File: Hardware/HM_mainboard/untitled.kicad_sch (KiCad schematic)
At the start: 19 parts, among them J1 JST PH2P ST90, Q1 PMOS AS3401, U1 MCP73831-2, U2 TC1262-33

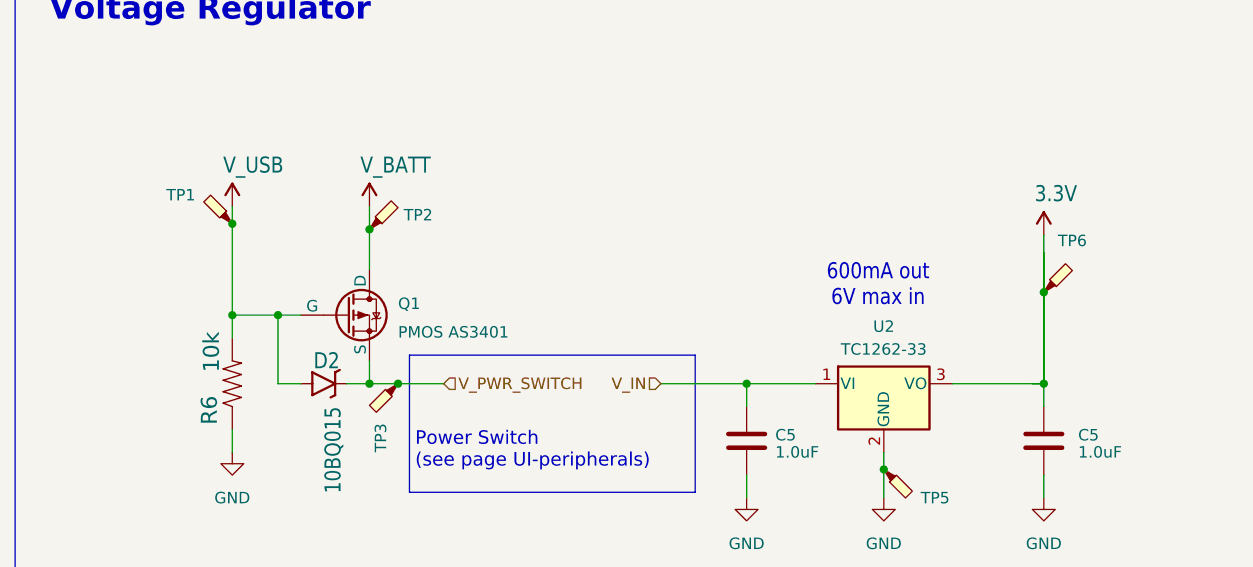
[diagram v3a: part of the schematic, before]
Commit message: Updated schematic to version v2.0.0
•	Removed two 6-Axis IMUs
•	As the BNO055 did not respond to I2C requests, a 2k7 pullup was added in parallel to the I2C-SDA pullup. The behavior is described here:  https://forums.adafruit.com/viewtopic.php?t=205215
•	Added mounting holes for enclosure
•	Added board description prints
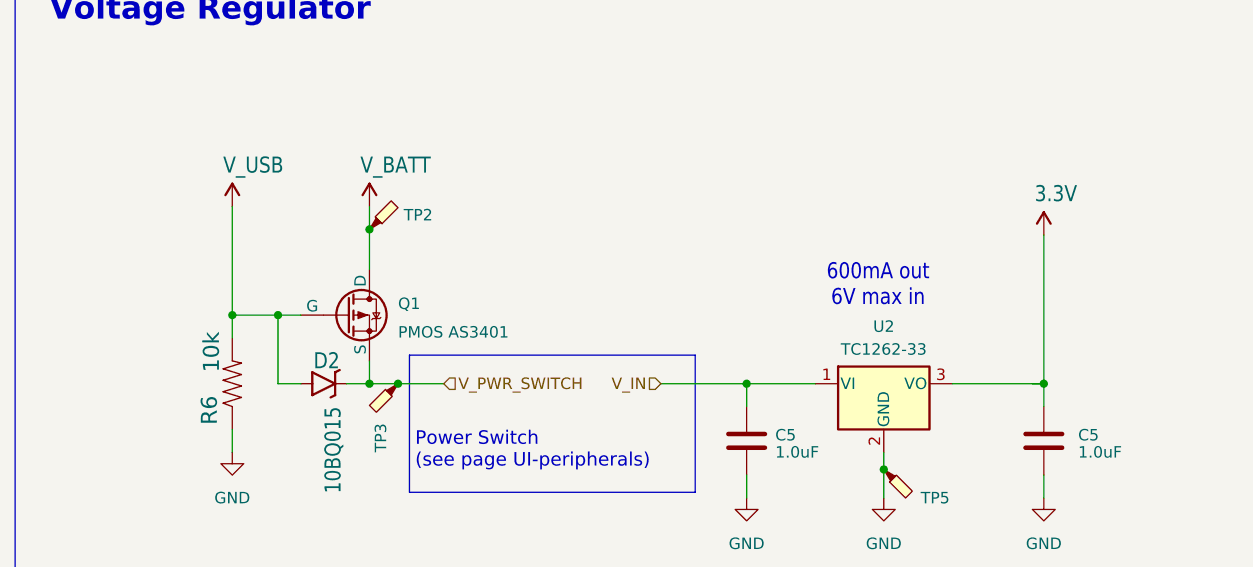
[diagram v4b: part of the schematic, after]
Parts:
- removed TP1: TestPoint_Probe, TestPoint:TestPoint_THTPad_D2.0mm_Drill1.0mm, symbol Connector:TestPoint_Probe
- removed TP6: 3v3, TestPoint:TestPoint_THTPad_D2.0mm_Drill1.0mm, symbol Connector:TestPoint_Probe
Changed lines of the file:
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@@
   (junction (at 109.855 149.86) (diameter 0) (color 0 0 0 0)
   )
-  (junction (at 44.45 47.625) (diameter 0) (color 0 0 0 0)
-  )
   (junction (at 59.69 65.405) (diameter 0) (color 0 0 0 0)
   )
@@
   (junction (at 49.53 57.785) (diameter 0) (color 0 0 0 0)
   )
-  (junction (at 134.62 55.245) (diameter 0) (color 0 0 0 0)
-  )
   (wire (pts (xy 63.5 155.575) (xy 65.405 155.575))
     (stroke (width 0) (type default))
@@
     (stroke (width 0) (type default))
   )
-  (wire (pts (xy 44.45 45.72) (xy 44.45 47.625))
-    (stroke (width 0.1524) (type solid))
-  )
-  (wire (pts (xy 44.45 47.625) (xy 44.45 57.785))
+  (wire (pts (xy 44.45 45.72) (xy 44.45 57.785))
     (stroke (width 0.1524) (type solid))
   )
@@
     (stroke (width 0.1524) (type solid))
   )
-  (wire (pts (xy 134.62 65.405) (xy 134.62 55.245))
-    (stroke (width 0.1524) (type solid))
-  )
   (wire (pts (xy 101.6 65.405) (xy 109.22 65.405))
     (stroke (width 0.1524) (type solid))
@@
     (stroke (width 0.1524) (type solid))
   )
-  (wire (pts (xy 134.62 48.895) (xy 134.62 55.245))
-    (stroke (width 0.1524) (type solid))
-  )
   (wire (pts (xy 134.62 65.405) (xy 133.35 65.405))
     (stroke (width 0) (type default))
@@
     (stroke (width 0) (type default))
   )
-  (wire (pts (xy 134.62 55.245) (xy 134.62 50.8))
-    (stroke (width 0) (type default))
-  )
   (wire (pts (xy 134.62 78.105) (xy 134.62 75.565))
     (stroke (width 0.1524) (type solid))
@@
     (stroke (width 0) (type default))
   )
-  (wire (pts (xy 134.62 55.245) (xy 134.62 65.405))
+  (wire (pts (xy 134.62 48.895) (xy 134.62 65.405))
     (stroke (width 0) (type default))
   )
@@
         )
         (path "/54a6df43-5475-46a2-9916-8b0260700d4c/b19d5209-4861-4a96-a3d1-daca4a23de52"
-          (reference "#SUPPLY026") (unit 1)
+          (reference "#SUPPLY03") (unit 1)
         )
       )
@@
         )
         (path "/54a6df43-5475-46a2-9916-8b0260700d4c/b19d5209-4861-4a96-a3d1-daca4a23de52"
-          (reference "#PWR08") (unit 1)
+          (reference "#PWR07") (unit 1)
         )
       )
@@
         )
         (path "/54a6df43-5475-46a2-9916-8b0260700d4c/b19d5209-4861-4a96-a3d1-daca4a23de52"
-          (reference "#PWR06") (unit 1)
+          (reference "#PWR05") (unit 1)
         )
       )
@@
         )
         (path "/54a6df43-5475-46a2-9916-8b0260700d4c/b19d5209-4861-4a96-a3d1-daca4a23de52"
-          (reference "#PWR04") (unit 1)
+          (reference "#PWR03") (unit 1)
         )
       )
@@
         )
         (path "/54a6df43-5475-46a2-9916-8b0260700d4c/b19d5209-4861-4a96-a3d1-daca4a23de52"
-          (reference "#PWR010") (unit 1)
+          (reference "#PWR09") (unit 1)
         )
       )
@@
         )
         (path "/54a6df43-5475-46a2-9916-8b0260700d4c/b19d5209-4861-4a96-a3d1-daca4a23de52"
-          (reference "#PWR09") (unit 1)
+          (reference "#PWR08") (unit 1)
         )
       )
@@
         )
         (path "/54a6df43-5475-46a2-9916-8b0260700d4c/b19d5209-4861-4a96-a3d1-daca4a23de52"
-          (reference "#PWR07") (unit 1)
+          (reference "#PWR06") (unit 1)
         )
       )
@@
         )
         (path "/54a6df43-5475-46a2-9916-8b0260700d4c/b19d5209-4861-4a96-a3d1-daca4a23de52"
-          (reference "#PWR05") (unit 1)
+          (reference "#PWR04") (unit 1)
         )
       )
@@
     )
   )
-  (symbol (lib_id "Connector:TestPoint_Probe") (at 134.62 55.245 0) (unit 1)
-    (in_bom yes) (on_board yes) (dnp no)
-    (property "Reference" "TP6" (at 137.795 49.53 0)
-      (effects (font (size 1.27 1.27)))
-    )
-    (property "Value" "3v3" (at 135.89 49.53 0)
-      (effects (font (size 1.27 1.27)) hide)
-    )
-    (property "Footprint" "TestPoint:TestPoint_THTPad_D2.0mm_Drill1.0mm" (at 139.7 55.245 0)
-      (effects (font (size 1.27 1.27)) hide)
-    )
-    (property "Datasheet" "~" (at 139.7 55.245 0)
-      (effects (font (size 1.27 1.27)) hide)
-    )
-    (pin "1")
-    (instances
-      (project "HM_mainboard"
-        (path "/54a6df43-5475-46a2-9916-8b0260700d4c/b19d5209-4861-4a96-a3d1-daca4a23de52"
-          (reference "TP6") (unit 1)
-        )
-      )
-    )
-  )
   (symbol (lib_id "Connector:TestPoint_Probe") (at 59.69 48.26 0) (unit 1)
     (in_bom yes) (on_board yes) (dnp no) (fields_autoplaced)
@@
         )
       )
-    )
-  )
-  (symbol (lib_id "Connector:TestPoint_Probe") (at 44.45 47.625 90) (unit 1)
-    (in_bom yes) (on_board yes) (dnp no)
-    (property "Reference" "TP1" (at 38.735 44.45 90)
-      (effects (font (size 1.27 1.27)))
-    )
-    (property "Value" "TestPoint_Probe" (at 33.02 46.355 90)
-      (effects (font (size 1.27 1.27)) hide)
-    )
-    (property "Footprint" "TestPoint:TestPoint_THTPad_D2.0mm_Drill1.0mm" (at 44.45 42.545 0)
-      (effects (font (size 1.27 1.27)) hide)
-    )
-    (property "Datasheet" "~" (at 44.45 42.545 0)
-      (effects (font (size 1.27 1.27)) hide)
-    )
-    (pin "1")
-    (instances
-      (project "HM_mainboard"
-        (path "/54a6df43-5475-46a2-9916-8b0260700d4c/b19d5209-4861-4a96-a3d1-daca4a23de52"
-          (reference "TP1") (unit 1)
-        )
-      )

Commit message: Added BOM, PDF and zipped V2.0.0 project data
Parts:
- removed TP3: TestPoint_Probe, TestPoint:TestPoint_THTPad_D2.0mm_Drill1.0mm, symbol Connector:TestPoint_Probe
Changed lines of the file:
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@@
   (junction (at 59.69 48.26) (diameter 0) (color 0 0 0 0)
   )
-  (junction (at 62.865 65.405) (diameter 0) (color 0 0 0 0)
-  )
   (junction (at 200.66 138.43) (diameter 0) (color 0 0 0 0)
   )
@@
     (stroke (width 0) (type default))
   )
-  (wire (pts (xy 62.865 65.405) (xy 67.945 65.405))
+  (wire (pts (xy 59.69 65.405) (xy 67.945 65.405))
     (stroke (width 0) (type default))
   )
@@
   (wire (pts (xy 82.55 149.86) (xy 82.55 153.67))
     (stroke (width 0.1524) (type solid))
-  )
-  (wire (pts (xy 59.69 65.405) (xy 62.865 65.405))
-    (stroke (width 0) (type default))
   )
   (wire (pts (xy 59.69 62.865) (xy 59.69 65.405))
@@
         )
       )
-    )
-  )
-  (symbol (lib_id "Connector:TestPoint_Probe") (at 62.865 65.405 180) (unit 1)
-    (in_bom yes) (on_board yes) (dnp no)
-    (property "Reference" "TP3" (at 60.96 73.025 90)
-      (effects (font (size 1.27 1.27)) (justify right))
-    )
-    (property "Value" "TestPoint_Probe" (at 62.865 84.455 90)
-      (effects (font (size 1.27 1.27)) (justify right) hide)
-    )
-    (property "Footprint" "TestPoint:TestPoint_THTPad_D2.0mm_Drill1.0mm" (at 57.785 65.405 0)
-      (effects (font (size 1.27 1.27)) hide)
-    )
-    (property "Datasheet" "~" (at 57.785 65.405 0)
-      (effects (font (size 1.27 1.27)) hide)
-    )
-    (pin "1")
-    (instances
-      (project "HM_mainboard"
-        (path "/54a6df43-5475-46a2-9916-8b0260700d4c/b19d5209-4861-4a96-a3d1-daca4a23de52"
-          (reference "TP3") (unit 1)
-        )
-      )

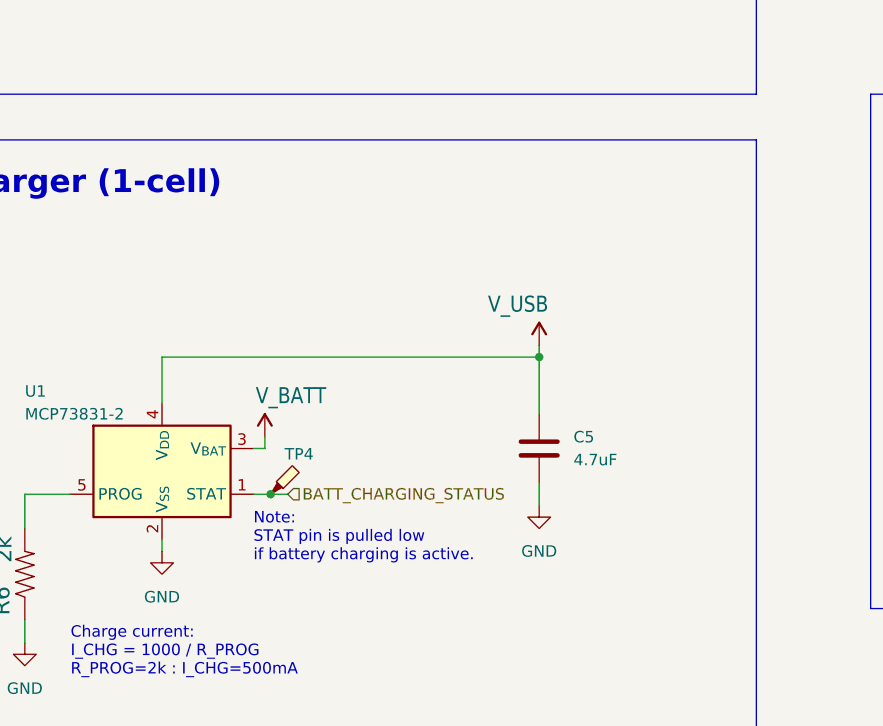
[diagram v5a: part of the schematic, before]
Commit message: Replaced weak pullup at battery charging status by 1k pullup
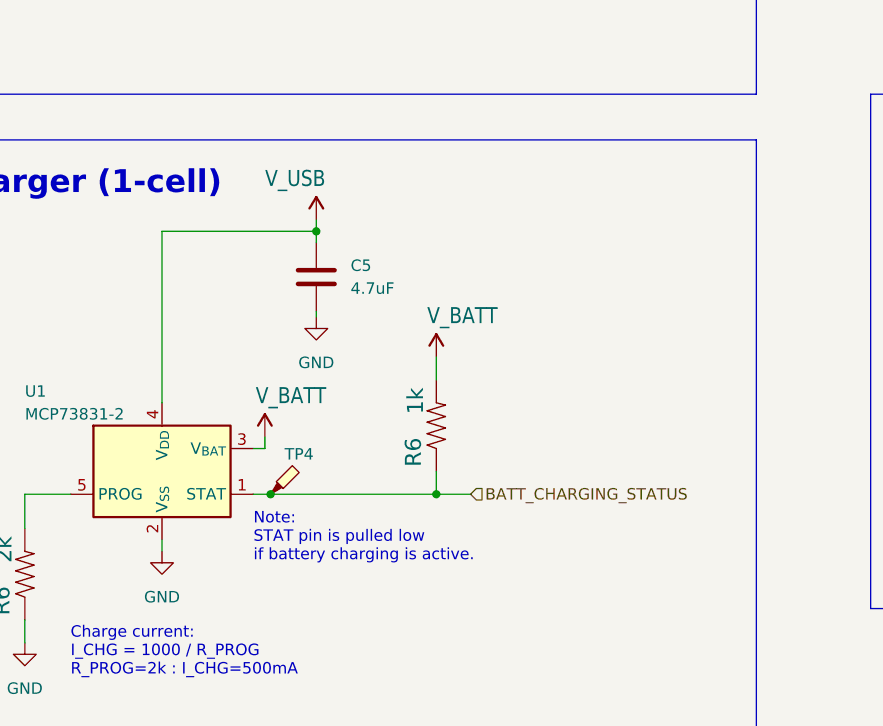
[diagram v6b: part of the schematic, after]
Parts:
- added R6: 1k, Resistor_SMD:R_0603_1608Metric_Pad0.98x0.95mm_HandSolder, symbol esp32-thing-eagle-import:27OHM1/10W1%(0603)0603-RES
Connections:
- net BATT_CHARGING_STATUS: now also R6.1
- net V_BATT: now also R6.2
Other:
- moved on the sheet: C5
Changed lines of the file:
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@@
   (junction (at 200.66 138.43) (diameter 0) (color 0 0 0 0)
   )
+  (junction (at 128.27 149.86) (diameter 0) (color 0 0 0 0)
+  )
   (junction (at 65.405 146.05) (diameter 0) (color 0 0 0 0)
   )
-  (junction (at 139.7 134.62) (diameter 0) (color 0 0 0 0)
+  (junction (at 114.935 120.65) (diameter 0) (color 0 0 0 0)
   )
   (junction (at 49.53 57.785) (diameter 0) (color 0 0 0 0)
@@
     (stroke (width 0.1524) (type solid))
   )
+  (wire (pts (xy 128.27 147.32) (xy 128.27 149.86))
+    (stroke (width 0) (type default))
+  )
   (wire (pts (xy 200.66 123.19) (xy 200.66 125.73))
     (stroke (width 0) (type default))
@@
     (stroke (width 0) (type default))
   )
-  (wire (pts (xy 97.79 134.62) (xy 97.79 139.7))
+  (wire (pts (xy 114.935 130.175) (xy 114.935 129.54))
+    (stroke (width 0.1524) (type solid))
+  )
+  (wire (pts (xy 109.855 149.86) (xy 128.27 149.86))
+    (stroke (width 0) (type default))
+  )
+  (wire (pts (xy 97.79 120.65) (xy 97.79 139.7))
     (stroke (width 0) (type default))
   )
@@
     (stroke (width 0) (type default))
   )
-  (wire (pts (xy 139.7 133.35) (xy 139.7 134.62))
+  (wire (pts (xy 114.935 119.38) (xy 114.935 120.65))
     (stroke (width 0) (type default))
   )
@@
     (stroke (width 0.1524) (type solid))
   )
-  (wire (pts (xy 139.7 134.62) (xy 139.7 140.97))
+  (wire (pts (xy 114.935 120.65) (xy 114.935 121.92))
     (stroke (width 0.1524) (type solid))
   )
@@
     (stroke (width 0.1524) (type solid))
   )
-  (wire (pts (xy 97.79 134.62) (xy 139.7 134.62))
+  (wire (pts (xy 97.79 120.65) (xy 114.935 120.65))
     (stroke (width 0) (type default))
   )
@@
     (stroke (width 0.1524) (type solid))
   )
-  (wire (pts (xy 139.7 151.13) (xy 139.7 148.59))
-    (stroke (width 0.1524) (type solid))
-  )
   (wire (pts (xy 57.15 65.405) (xy 59.69 65.405))
     (stroke (width 0) (type default))
@@
     (stroke (width 0) (type default))
   )
+  (wire (pts (xy 128.27 134.62) (xy 128.27 137.16))
+    (stroke (width 0) (type default))
+  )
   (wire (pts (xy 134.62 78.105) (xy 134.62 75.565))
     (stroke (width 0.1524) (type solid))
@@
     (stroke (width 0.1524) (type solid))
   )
-  (wire (pts (xy 111.76 149.86) (xy 109.855 149.86))
+  (wire (pts (xy 132.08 149.86) (xy 128.27 149.86))
     (stroke (width 0) (type default))
   )
@@
     (effects (font (size 2.54 2.54) (thickness 0.508) bold) (justify left bottom))
   )
-  (hierarchical_label "BATT_CHARGING_STATUS" (shape input) (at 111.76 149.86 0) (fields_autoplaced)
+  (hierarchical_label "BATT_CHARGING_STATUS" (shape input) (at 132.08 149.86 0) (fields_autoplaced)
     (effects (font (size 1.27 1.27)) (justify left))
   )
@@
     )
   )
-  (symbol (lib_id "esp32-thing-eagle-import:V_USB") (at 139.7 133.35 0) (mirror y) (unit 1)
-    (in_bom yes) (on_board yes) (dnp no)
-    (property "Reference" "#SUPPLY06" (at 139.7 133.35 0)
-      (effects (font (size 1.27 1.27)) hide)
-    )
-    (property "Value" "V_USB" (at 140.716 129.794 0)
+  (symbol (lib_id "esp32-thing-eagle-import:V_USB") (at 114.935 119.38 0) (mirror y) (unit 1)
+    (in_bom yes) (on_board yes) (dnp no)
+    (property "Reference" "#SUPPLY06" (at 114.935 119.38 0)
+      (effects (font (size 1.27 1.27)) hide)
+    )
+    (property "Value" "V_USB" (at 115.951 115.824 0)
       (effects (font (size 1.778 1.5113)) (justify left bottom))
     )
-    (property "Footprint" "" (at 139.7 133.35 0)
-      (effects (font (size 1.27 1.27)) hide)
-    )
-    (property "Datasheet" "" (at 139.7 133.35 0)
+    (property "Footprint" "" (at 114.935 119.38 0)
+      (effects (font (size 1.27 1.27)) hide)
+    )
+    (property "Datasheet" "" (at 114.935 119.38 0)
       (effects (font (size 1.27 1.27)) hide)
     )
@@
     )
   )
-  (symbol (lib_name "GND_1") (lib_id "power:GND") (at 139.7 151.13 0) (unit 1)
+  (symbol (lib_name "GND_1") (lib_id "power:GND") (at 114.935 130.175 0) (unit 1)
     (in_bom yes) (on_board yes) (dnp no) (fields_autoplaced)
-    (property "Reference" "#PWR06" (at 139.7 157.48 0)
-      (effects (font (size 1.27 1.27)) hide)
-    )
-    (property "Value" "GND" (at 139.7 156.21 0)
+    (property "Reference" "#PWR06" (at 114.935 136.525 0)
+      (effects (font (size 1.27 1.27)) hide)
+    )
+    (property "Value" "GND" (at 114.935 135.255 0)
       (effects (font (size 1.27 1.27)))
     )
-    (property "Footprint" "" (at 139.7 151.13 0)
-      (effects (font (size 1.27 1.27)) hide)
-    )
-    (property "Datasheet" "" (at 139.7 151.13 0)
+    (property "Footprint" "" (at 114.935 130.175 0)
+      (effects (font (size 1.27 1.27)) hide)
+    )
+    (property "Datasheet" "" (at 114.935 130.175 0)
       (effects (font (size 1.27 1.27)) hide)
     )
@@
     )
   )
-  (symbol (lib_id "Device:C") (at 139.7 144.78 0) (unit 1)
+  (symbol (lib_id "Device:C") (at 114.935 125.73 0) (unit 1)
     (in_bom yes) (on_board yes) (dnp no) (fields_autoplaced)
-    (property "Reference" "C5" (at 143.51 143.51 0)
+    (property "Reference" "C5" (at 118.745 124.46 0)
       (effects (font (size 1.27 1.27)) (justify left))
     )
-    (property "Value" "4.7uF" (at 143.51 146.05 0)
+    (property "Value" "4.7uF" (at 118.745 127 0)
       (effects (font (size 1.27 1.27)) (justify left))
     )
-    (property "Footprint" "Capacitor_SMD:C_0603_1608Metric_Pad1.08x0.95mm_HandSolder" (at 140.6652 148.59 0)
-      (effects (font (size 1.27 1.27)) hide)
-    )
-    (property "Datasheet" "~" (at 139.7 144.78 0)
-      (effects (font (size 1.27 1.27)) hide)
-    )
-    (property "Reichelt" "" (at 139.7 144.78 0)
+    (property "Footprint" "Capacitor_SMD:C_0603_1608Metric_Pad1.08x0.95mm_HandSolder" (at 115.9002 129.54 0)
+      (effects (font (size 1.27 1.27)) hide)
+    )
+    (property "Datasheet" "~" (at 114.935 125.73 0)
+      (effects (font (size 1.27 1.27)) hide)
+    )
+    (property "Reichelt" "" (at 114.935 125.73 0)
       (effects (font (size 1.27 1.27)) hide)
     )
@@
     )
   )
+  (symbol (lib_id "esp32-thing-eagle-import:27OHM1/10W1%(0603)0603-RES") (at 128.27 142.24 90) (unit 1)
+    (in_bom yes) (on_board yes) (dnp no)
+    (property "Reference" "R6" (at 126.7714 146.812 0)
+      (effects (font (size 1.778 1.778)) (justify left bottom))
+    )
+    (property "Value" "1k" (at 127 140.97 0)
+      (effects (font (size 1.778 1.778)) (justify left bottom))
+    )
+    (property "Footprint" "Resistor_SMD:R_0603_1608Metric_Pad0.98x0.95mm_HandSolder" (at 128.27 142.24 0)
+      (effects (font (size 1.27 1.27)) hide)
+    )
+    (property "Datasheet" "" (at 128.27 142.24 0)
+      (effects (font (size 1.27 1.27)) hide)
+    )
+    (property "Mouser" "ERJ-PA3J121V" (at 128.27 142.24 0)
+      (effects (font (size 1.27 1.27)) hide)
+    )
+    (property "Reichelt" "" (at 128.27 142.24 0)
+      (effects (font (size 1.27 1.27)) hide)
+    )
+    (pin "1")
+    (pin "2")
+    (instances
+      (project "HM_mainboard"
+        (path "/54a6df43-5475-46a2-9916-8b0260700d4c"
+          (reference "R6") (unit 1)
+        )
+        (path "/54a6df43-5475-46a2-9916-8b0260700d4c/8a725ce3-408a-4762-9df2-b56094186e56"
+          (reference "R14") (unit 1)
+        )
+        (path "/54a6df43-5475-46a2-9916-8b0260700d4c/137c5701-d01e-40ce-919d-b371cfda41da"
+          (reference "R11") (unit 1)
+        )
+        (path "/54a6df43-5475-46a2-9916-8b0260700d4c/b19d5209-4861-4a96-a3d1-daca4a23de52"
+          (reference "R16") (unit 1)
+        )
+      )
+      (project "esp32-thing"
+        (path "/64c5aff3-bdec-4fb6-b5ec-87e5efa2adf7"
+          (reference "R13") (unit 1)
+        )
+      )
+    )
+  )
   (symbol (lib_id "esp32-thing-eagle-import:V_USB") (at 44.45 45.72 0) (unit 1)
     (in_bom yes) (on_board yes) (dnp no)
@@
         )
       )
+    )
+  )
+  (symbol (lib_id "esp32-thing-eagle-import:V_BATT") (at 128.27 134.62 0) (unit 1)
+    (in_bom yes) (on_board yes) (dnp no)
+    (property "Reference" "#SUPPLY02" (at 128.27 134.62 0)
+      (effects (font (size 1.27 1.27)) hide)
+    )
+    (property "Value" "V_BATT" (at 127.254 131.064 0)
+      (effects (font (size 1.778 1.5113)) (justify left bottom))
+    )
+    (property "Footprint" "" (at 128.27 134.62 0)
+      (effects (font (size 1.27 1.27)) hide)
+    )
+    (property "Datasheet" "" (at 128.27 134.62 0)
+      (effects (font (size 1.27 1.27)) hide)
+    )
+    (pin "1")
+    (instances
+      (project "HM_mainboard"
+        (path "/54a6df43-5475-46a2-9916-8b0260700d4c"
+          (reference "#SUPPLY02") (unit 1)
+        )
+        (path "/54a6df43-5475-46a2-9916-8b0260700d4c/b19d5209-4861-4a96-a3d1-daca4a23de52"
+          (reference "#SUPPLY012") (unit 1)
+        )
+      )
+      (project "esp32-thing"
+        (path "/64c5aff3-bdec-4fb6-b5ec-87e5efa2adf7"
+          (reference "#SUPPLY27") (unit 1)
+        )
+      )
